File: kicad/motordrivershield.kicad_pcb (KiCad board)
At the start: 2 copper layers, 100 x 60 mm, 153 parts, among them CN1 ARDUINO_MKR, CN2 QWIIC, CN3 ARDUINO_NANO_33, P1 CONN_01X03, P2 CONN_01X03, P5 WR-TBL_691313710002, P6 WR-TBL_691313710002, P7 CONN_01X02, P8 WR-TBL_691313710002, U1 PCA9685_TSSOP28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

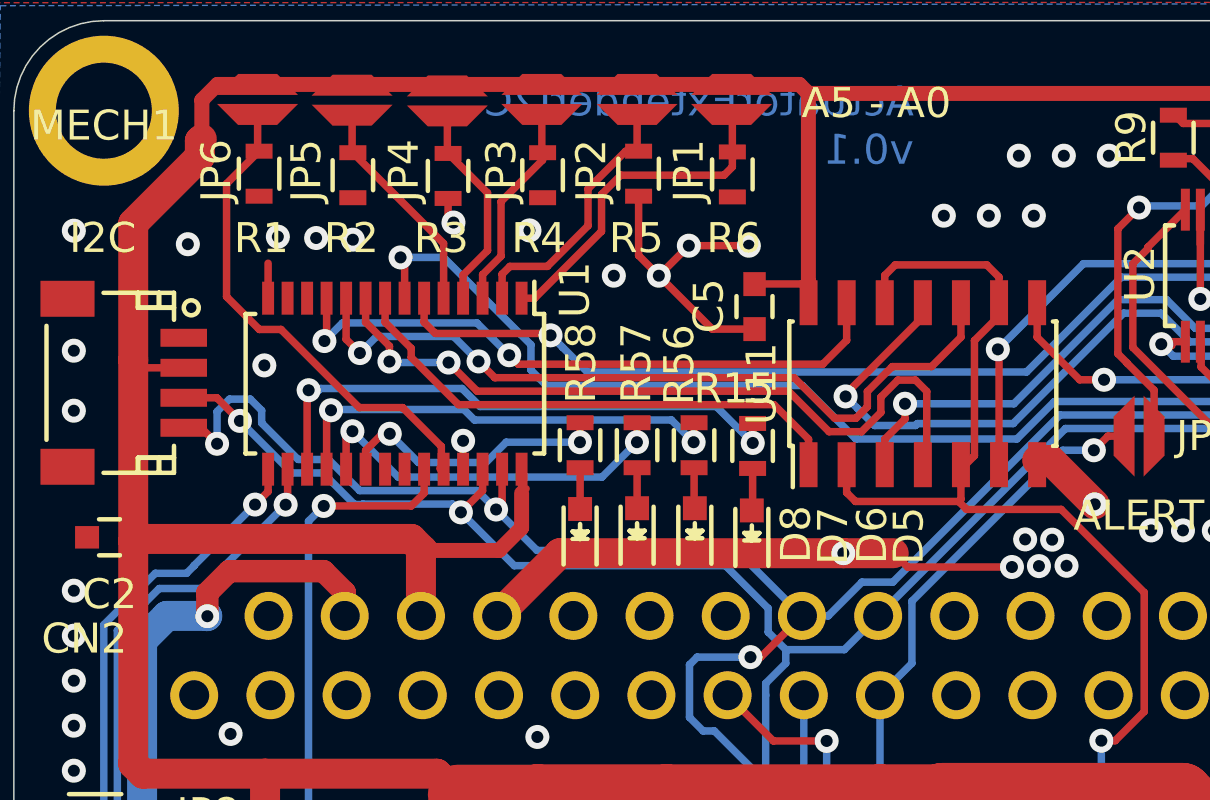
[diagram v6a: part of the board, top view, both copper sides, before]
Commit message: swapped sda and scl on pca9685
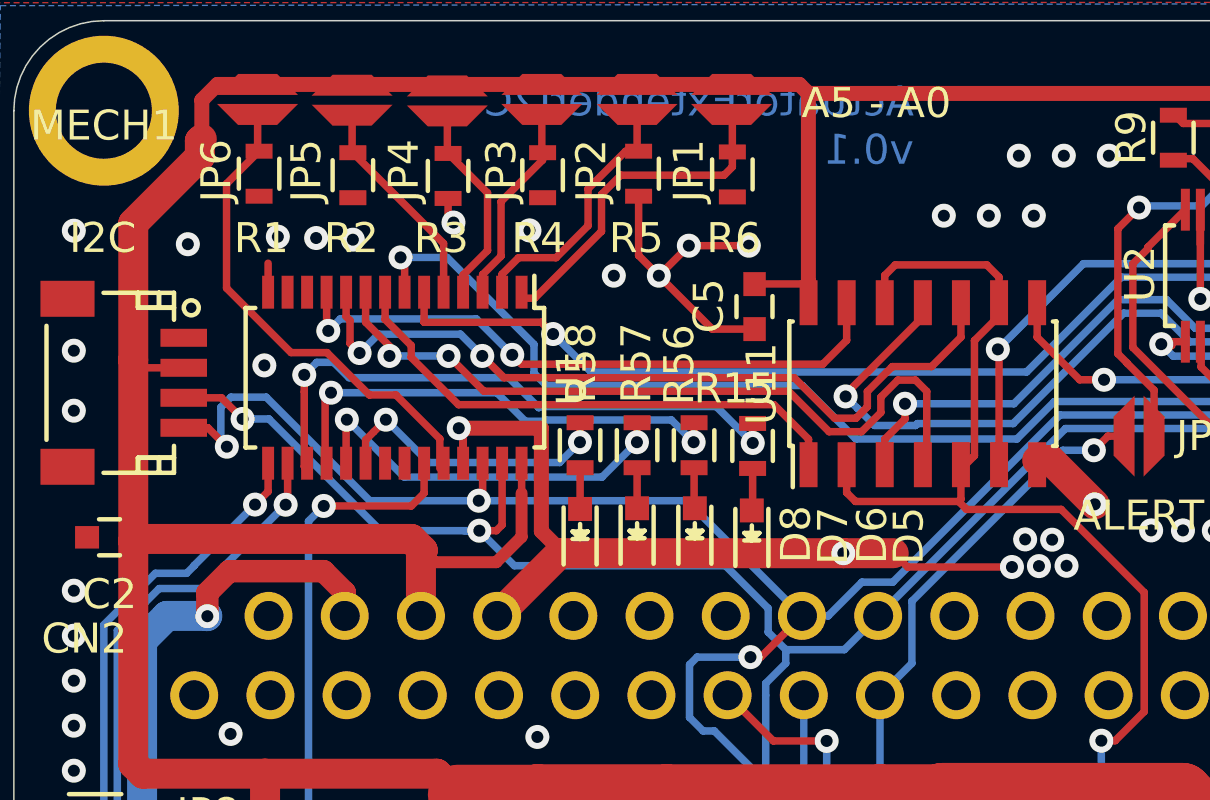
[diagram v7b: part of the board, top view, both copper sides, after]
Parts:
- moved U1 0.20 mm to (102.7, 51.9)
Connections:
- U1 pad 26: /SDA -> /SCL
- U1 pad 27: /SCL -> /SDA
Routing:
- net GND: track 142.3 -> 150.7 mm
- net /SDA: track 70.5 -> 72.2 mm
- net Net-(R15-Pad2): track 18.9 -> 20.1 mm
- net Net-(R56-Pad2): track 15.2 -> 16.1 mm
- net Net-(R57-Pad2): track 12.6 -> 13.3 mm
- net Net-(R58-Pad2): track 9.33 -> 9.92 mm
- net PWM4: track 21.1 -> 20.6 mm

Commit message: blöden servo wegen kompass gemacht
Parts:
- added R14: 0R0, resistors:R_0603, F.Cu at (105.2, 83.6)
- added R55: 0R0, resistors:R_0603, F.Cu at (114.6, 86.2)
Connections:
- net Net-(R12-Pad2) renamed /SERVO0_PCA
- net Net-(R13-Pad2) renamed /SERVO1_PCA
- net SERVO0 renamed Net-(P1-Pad1)
- net SERVO1 renamed Net-(P2-Pad1)
- CN1 pad 3: (no net) -> /SERVO0_MCU
- CN1 pad 5: (no net) -> /SERVO1_MCU
- CN3 pad 5: (no net) -> /SERVO0_MCU
- CN3 pad 7: (no net) -> /SERVO1_MCU
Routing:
- net /SERVO1_MCU: track 0.00 -> 11.8 mm
- net /SERVO0_MCU: track 0.00 -> 6.98 mm
- net Net-(P1-Pad1): track 2.45 -> 6.26 mm
- net Net-(P2-Pad1): track 2.53 -> 4.64 mm
- net GND: vias 220 -> 223
